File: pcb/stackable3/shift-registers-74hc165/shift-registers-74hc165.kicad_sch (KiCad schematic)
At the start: 30 parts, among them J1 Pin headers, J2 Pin socket, J3 Pin headers, J6 JST SH, J7 JST SH, Q1 AO3401A, SW0 SW_SPDT_MountingPin, SW1 Tactile, right-angle, SW2 Tactile 3.3mm, SW3 Tactile 3.3mm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

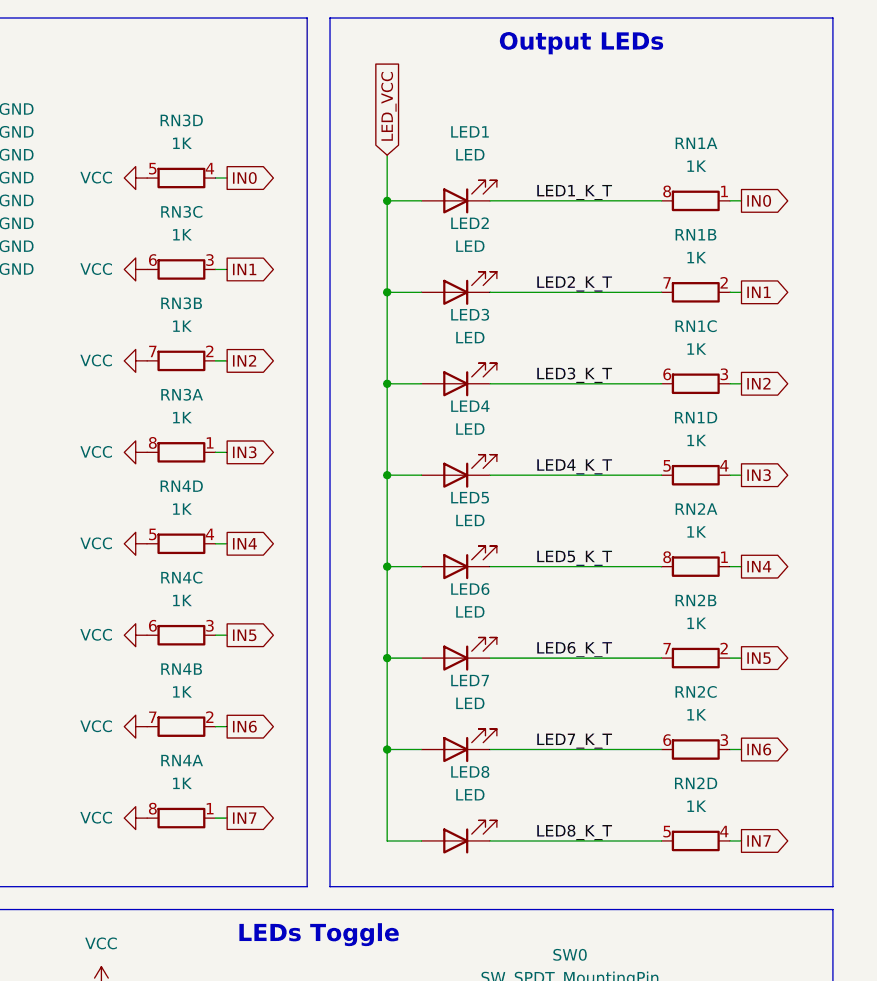
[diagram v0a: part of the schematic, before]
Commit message: Add more LCSC part numbers on stackable3/shift-registers-74hc165
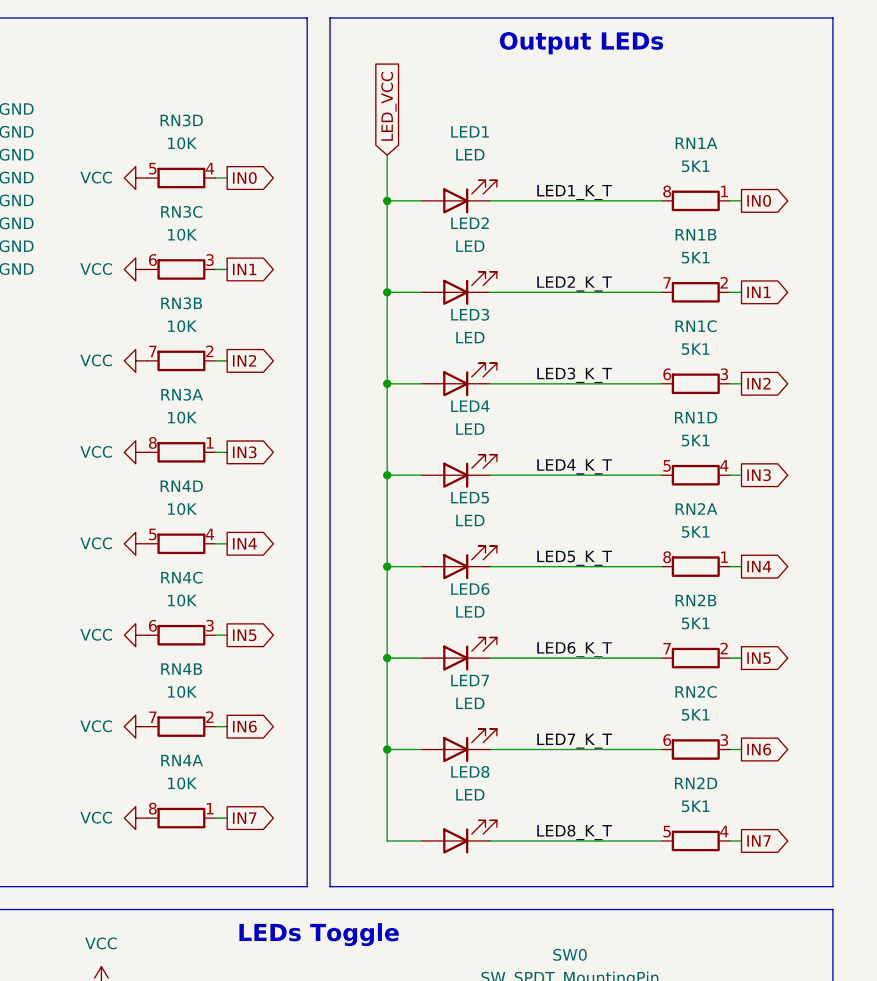
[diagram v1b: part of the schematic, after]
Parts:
- RN0: LCSC Part (none) -> C110924
- RN1, RN2: value 1K -> 5K1; LCSC Part (none) -> C425290
- RN3, RN4: value 1K -> 10K; LCSC Part (none) -> C7422173
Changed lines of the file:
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@@
 			)
 		)
-		(property "Value" "1K"
+		(property "Value" "5K1"
 			(at 266.7 41.91 90)
 			(effects
@@
 			)
 		)
+		(property "LCSC Part" "C425290"
+			(at 266.7 45.72 90)
+			(effects
+				(font
+					(size 1.27 1.27)
+				)
+				(hide yes)
+			)
+		)
 		(pin "4"
 		)
@@
 			)
 		)
-		(property "Value" "1K"
+		(property "Value" "10K"
 			(at 209.55 59.69 90)
 			(effects
@@
 			)
 		)
+		(property "LCSC Part" "C7422173"
+			(at 209.55 63.5 90)
+			(effects
+				(font
+					(size 1.27 1.27)
+				)
+				(hide yes)
+			)
+		)
 		(pin "4"
 		)
@@
 			)
 		)
-		(property "Value" "1K"
+		(property "Value" "10K"
 			(at 209.55 69.85 90)
 			(effects
@@
 			)
 		)
+		(property "LCSC Part" "C7422173"
+			(at 209.55 73.66 90)
+			(effects
+				(font
+					(size 1.27 1.27)
+				)
+				(hide yes)
+			)
+		)
 		(pin "4"
 		)
@@
 			)
 		)
+		(property "LCSC Part" "C110924"
+			(at 81.28 69.85 90)
+			(effects
+				(font
+					(size 1.27 1.27)
+				)
+				(hide yes)
+			)
+		)
 		(pin "4"
 		)
@@
 			)
 		)
-		(property "Value" "1K"
+		(property "Value" "10K"
 			(at 209.55 100.33 90)
 			(effects
@@
 			)
 		)
+		(property "LCSC Part" "C7422173"
+			(at 209.55 104.14 90)
+			(effects
+				(font
+					(size 1.27 1.27)
+				)
+				(hide yes)
+			)
+		)
 		(pin "4"
 		)
@@
 			)
 		)
-		(property "Value" "1K"
+		(property "Value" "10K"
 			(at 209.55 49.53 90)
 			(effects
@@
 			)
 		)
+		(property "LCSC Part" "C7422173"
+			(at 209.55 53.34 90)
+			(effects
+				(font
+					(size 1.27 1.27)
+				)
+				(hide yes)
+			)
+		)
 		(pin "4"
 		)
@@
 			)
 		)
-		(property "Value" "1K"
+		(property "Value" "10K"
 			(at 209.55 90.17 90)
 			(effects
@@
 			)
 		)
+		(property "LCSC Part" "C7422173"
+			(at 209.55 93.98 90)
+			(effects
+				(font
+					(size 1.27 1.27)
+				)
+				(hide yes)
+			)
+		)
 		(pin "4"
 		)
@@
 			)
 		)
-		(property "Value" "1K"
+		(property "Value" "10K"
 			(at 209.55 80.01 90)
 			(effects
@@
 			)
 		)
+		(property "LCSC Part" "C7422173"
+			(at 209.55 83.82 90)
+			(effects
+				(font
+					(size 1.27 1.27)
+				)
+				(hide yes)
+			)
+		)
 		(pin "4"
 		)
@@
 			)
 		)
-		(property "Value" "1K"
+		(property "Value" "5K1"
 			(at 266.7 31.75 90)
 			(effects
@@
 			)
 		)
+		(property "LCSC Part" "C425290"
+			(at 266.7 35.56 90)
+			(effects
+				(font
+					(size 1.27 1.27)
+				)
+				(hide yes)
+			)
+		)
 		(pin "4"
 		)
@@
 			)
 		)
-		(property "Value" "1K"
+		(property "Value" "5K1"
 			(at 266.7 62.23 90)
 			(effects
@@
 			)
 		)
+		(property "LCSC Part" "C425290"
+			(at 266.7 66.04 90)
+			(effects
+				(font
+					(size 1.27 1.27)
+				)
+				(hide yes)
+			)
+		)
 		(pin "4"
 		)
@@
 			)
 		)
+		(property "LCSC Part" "C110924"
+			(at 81.28 80.01 90)
+			(effects
+				(font
+					(size 1.27 1.27)
+				)
+				(hide yes)
+			)
+		)
 		(pin "4"
 		)
@@
 			)
 		)
-		(property "Value" "1K"
+		(property "Value" "5K1"
 			(at 266.7 72.39 90)
 			(effects
@@
 			)
 		)
+		(property "LCSC Part" "C425290"
+			(at 266.7 76.2 90)
+			(effects
+				(font
+					(size 1.27 1.27)
+				)
+				(hide yes)
+			)
+		)
 		(pin "4"
 		)
@@
 			)
 		)
+		(property "LCSC Part" "C110924"
+			(at 81.28 90.17 90)
+			(effects
+				(font
+					(size 1.27 1.27)
+				)
+				(hide yes)
+			)
+		)
 		(pin "4"
 		)
@@
 			)
 		)
-		(property "Value" "1K"
+		(property "Value" "5K1"
 			(at 266.7 102.87 90)
 			(effects
@@
 			)
 		)
+		(property "LCSC Part" "C425290"
+			(at 266.7 106.68 90)
+			(effects
+				(font
+					(size 1.27 1.27)
+				)
+				(hide yes)
+			)
+		)
 		(pin "4"
 		)
@@
 			)
 		)
-		(property "Value" "1K"
+		(property "Value" "10K"
 			(at 209.55 39.37 90)
 			(effects
@@
 			)
 		)
+		(property "LCSC Part" "C7422173"
+			(at 209.55 43.18 90)
+			(effects
+				(font
+					(size 1.27 1.27)
+				)
+				(hide yes)
+			)
+		)
 		(pin "4"
 		)
@@
 			)
 		)
-		(property "Value" "1K"
+		(property "Value" "5K1"
 			(at 266.7 92.71 90)
 			(effects
@@
 			)
 		)
+		(property "LCSC Part" "C425290"
+			(at 266.7 96.52 90)
+			(effects
+				(font
+					(size 1.27 1.27)
+				)
+				(hide yes)
+			)
+		)
 		(pin "4"
 		)
@@
 			)
 		)
-		(property "Value" "1K"
+		(property "Value" "5K1"
 			(at 266.7 82.55 90)
 			(effects
@@
 			)
 		)
+		(property "LCSC Part" "C425290"
+			(at 266.7 86.36 90)
+			(effects
+				(font
+					(size 1.27 1.27)
+				)
+				(hide yes)
+			)
+		)
 		(pin "4"
 		)
@@
 			)
 		)
-		(property "Value" "1K"
+		(property "Value" "10K"
 			(at 209.55 29.21 90)
 			(effects
@@
 			)
 		)
+		(property "LCSC Part" "C7422173"
+			(at 209.55 33.02 90)
+			(effects
+				(font
+					(size 1.27 1.27)
+				)
+				(hide yes)
+			)
+		)
 		(pin "4"
 		)
@@
 			)
 		)
+		(property "LCSC Part" "C110924"
+			(at 81.28 100.33 90)
+			(effects
+				(font
+					(size 1.27 1.27)
+				)
+				(hide yes)
+			)
+		)
 		(pin "4"
 		)
@@
 			)
 		)
-		(property "Value" "1K"
+		(property "Value" "5K1"
 			(at 266.7 52.07 90)
 			(effects
@@
 			(effects
 				(font
+					(size 1.27 1.27)
+				)
+				(hide yes)
+			)
+		)
+		(property "LCSC Part" "C425290"
+			(at 266.7 55.88 90)
+			(effects
+				(font

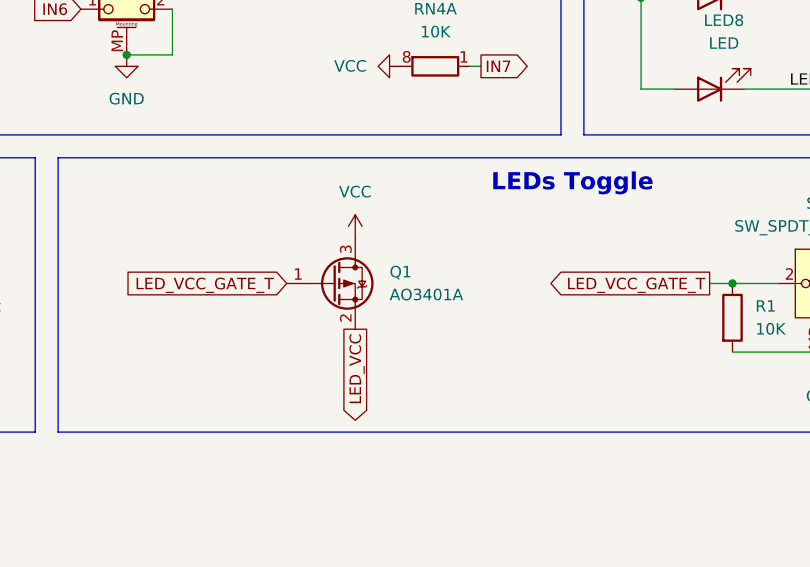
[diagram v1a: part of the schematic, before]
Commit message: Fix LEDs MOSFET direction in stackable3/shift-registers-74hc165 circuit
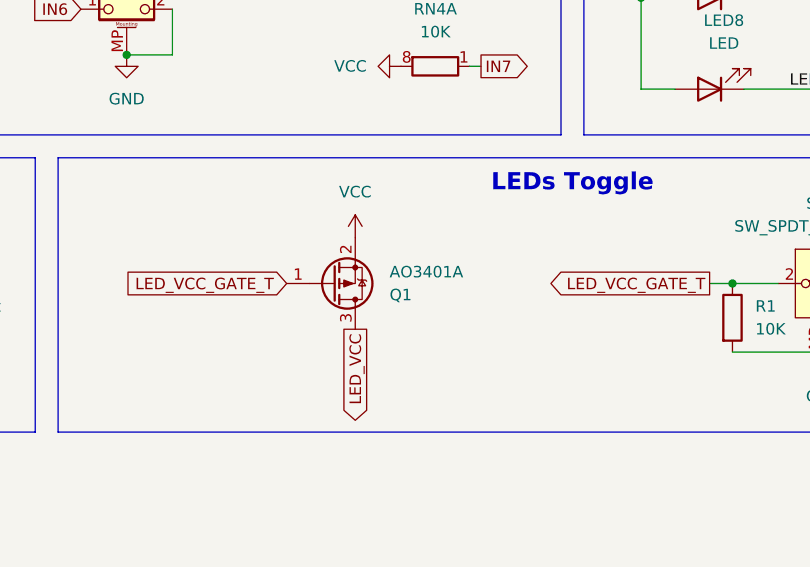
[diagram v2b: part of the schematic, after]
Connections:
- net LED_VCC: now also Q1.3 (D); no longer Q1.2 (S)
- net VCC: now also Q1.2 (S); no longer Q1.3 (D)
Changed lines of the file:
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@@
 		(lib_id "Transistor_FET:AO3401A")
 		(at 198.12 128.27 0)
+		(mirror x)
 		(unit 1)
 		(exclude_from_sim no)
@@
 		(fields_autoplaced yes)
 		(property "Reference" "Q1"
-			(at 204.47 126.9999 0)
+			(at 204.47 129.5401 0)
 			(effects
 				(font
@@
 		)
 		(property "Value" "AO3401A"
-			(at 204.47 129.5399 0)
+			(at 204.47 127.0001 0)
 			(effects
 				(font
@@
 		)
 		(property "Footprint" "Package_TO_SOT_SMD:SOT-23"
-			(at 203.2 130.175 0)
+			(at 203.2 126.365 0)
 			(effects
 				(font
@@
 		)
 		(property "Datasheet" "http://www.aosmd.com/pdfs/datasheet/AO3401A.pdf"
-			(at 203.2 132.08 0)
+			(at 203.2 124.46 0)
 			(effects
 				(font
